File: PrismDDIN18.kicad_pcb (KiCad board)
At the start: 2 copper layers, 280 x 60 mm, 93 parts, among them CON1 BARREL_JACK, IC1 LM2596T-5, J1 Conn_01x03, M1 IN-18, M10 IN-18, Q2 2N7000, Q3 2N7000, Q4 2N7000, Q5 2N7000, Q6 IRF540N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

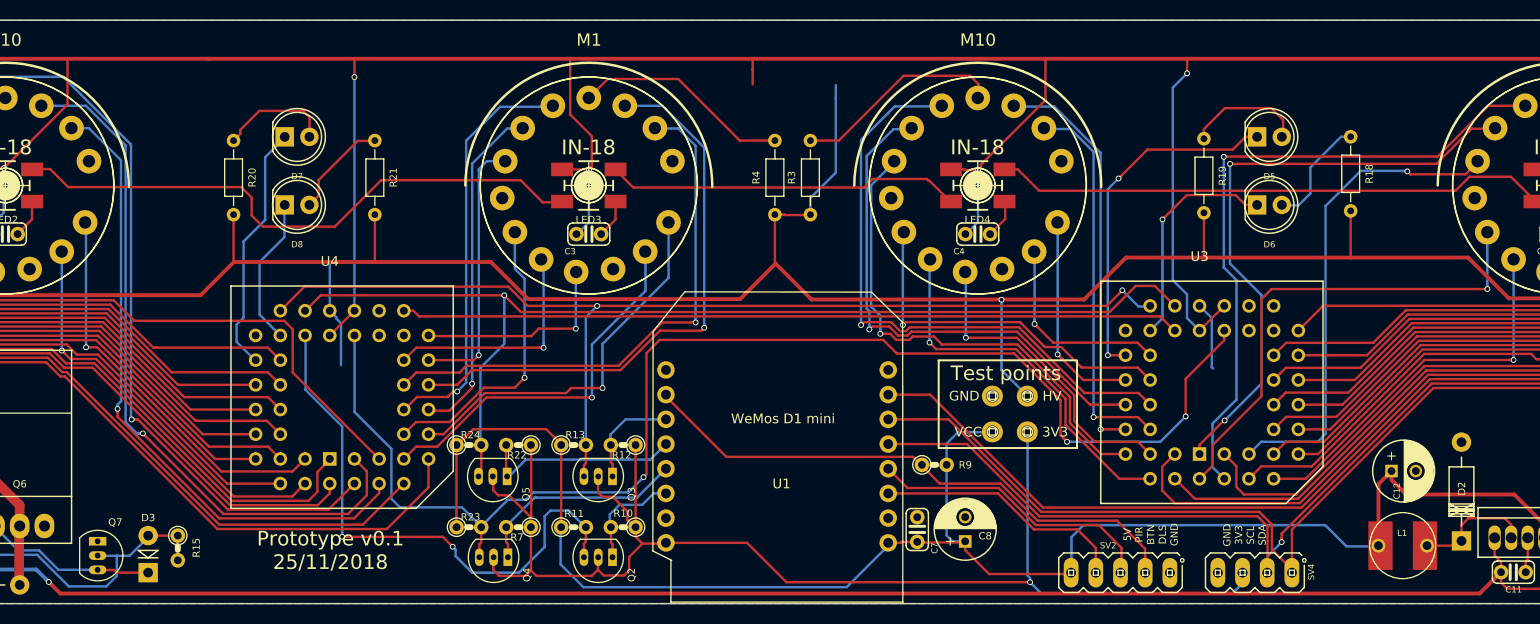
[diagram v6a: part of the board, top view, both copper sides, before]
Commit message: Add centre mouting hole
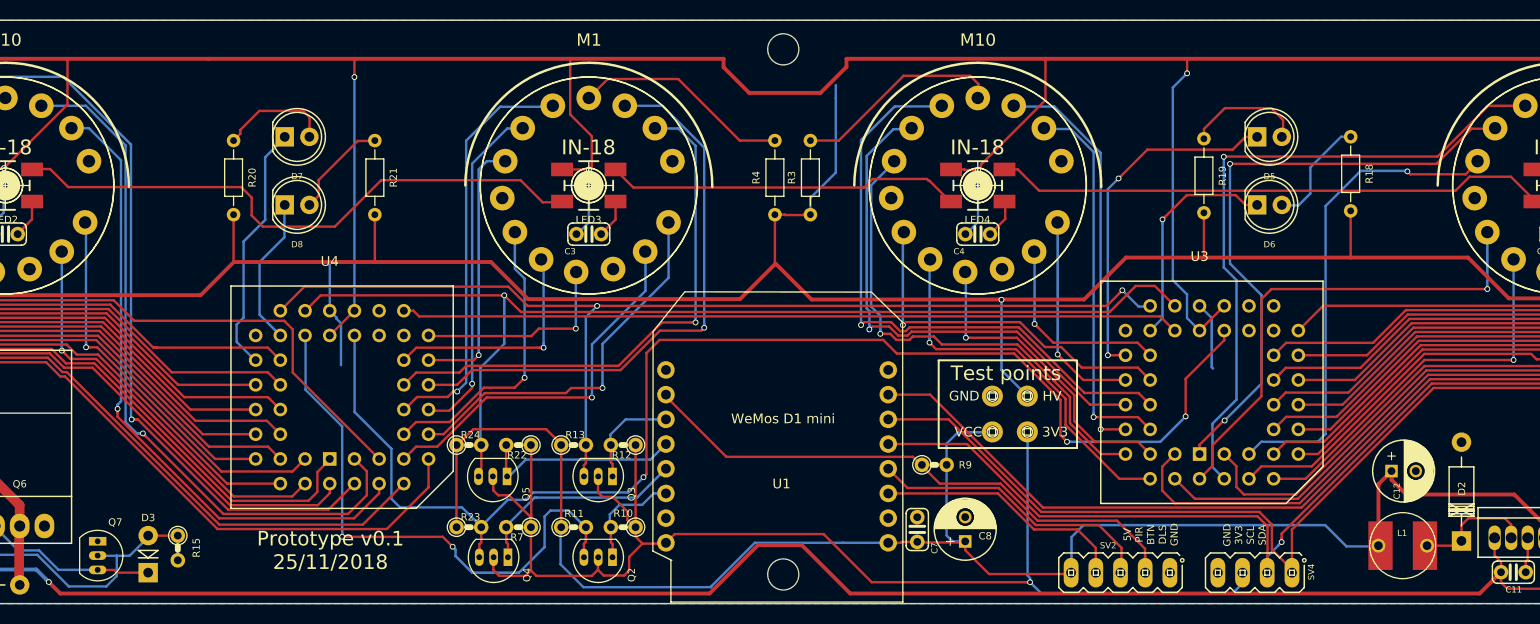
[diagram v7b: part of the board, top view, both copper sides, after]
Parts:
- added MH1: MountingHole_3.2mm_M3, NixieClockMaster:MountingHole_3.2mm_M3, F.Cu at (220.0, 109.0)
- added MH1: MountingHole_3.2mm_M3, NixieClockMaster:MountingHole_3.2mm_M3, F.Cu at (220.0, 163.0)
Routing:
- net /PWR_VIN: track 226.0 -> 230.1 mm
- net /VCC: track 778.1 -> 779.5 mm
- net /3V3: track 140.0 -> 140.8 mm
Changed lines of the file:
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@@
     (thickness 1.6)
     (drawings 17)
-    (tracks 1351)
+    (tracks 1362)
     (zones 0)
-    (modules 93)
+    (modules 95)
     (nets 125)
   )
@@
     (add_net "Net-(U5-Pad7)")
   )
+  (module NixieClockMaster:MountingHole_3.2mm_M3 (layer F.Cu)
+    (at 220 109)
+    (descr "Mounting Hole 3.2mm, no annular, M3")
+    (tags "mounting hole 3.2mm no annular m3")
+    (attr virtual)
+    (fp_text reference MH1 (at 0 -4.2) (layer F.Fab)
+      (effects (font (size 1 1) (thickness 0.15)))
+    )
+    (fp_text value MountingHole_3.2mm_M3 (at 0 4.2) (layer F.Fab)
+      (effects (font (size 1 1) (thickness 0.15)))
+    )
+    (fp_text user %R (at 0.3 0) (layer F.Fab)
+      (effects (font (size 1 1) (thickness 0.15)))
+    )
+    (fp_circle (center 0 0) (end 3.2 0) (layer Cmts.User) (width 0.15))
+    (fp_circle (center 0 0) (end 3.45 0) (layer F.CrtYd) (width 0.05))
+    (pad 1 np_thru_hole circle (at 0 0) (size 3.2 3.2) (drill 3.2) (layers *.Cu *.Mask))
+  )
+  (module NixieClockMaster:MountingHole_3.2mm_M3 (layer F.Cu)
+    (at 220 163)
+    (descr "Mounting Hole 3.2mm, no annular, M3")
+    (tags "mounting hole 3.2mm no annular m3")
+    (attr virtual)
+    (fp_text reference MH1 (at 0 -4.2) (layer F.Fab)
+      (effects (font (size 1 1) (thickness 0.15)))
+    )
+    (fp_text value MountingHole_3.2mm_M3 (at 0 4.2) (layer F.Fab)
+      (effects (font (size 1 1) (thickness 0.15)))
+    )
+    (fp_circle (center 0 0) (end 3.45 0) (layer F.CrtYd) (width 0.05))
+    (fp_circle (center 0 0) (end 3.2 0) (layer Cmts.User) (width 0.15))
+    (fp_text user %R (at 0.3 0) (layer F.Fab)
+      (effects (font (size 1 1) (thickness 0.15)))
+    )
+    (pad 1 np_thru_hole circle (at 0 0) (size 3.2 3.2) (drill 3.2) (layers *.Cu *.Mask))
+  )
   (module NixieClockMaster:C025-024X044 (layer F.Cu)
     (at 100 128)
@@
   (segment (start 241.17 162.96) (end 249.7 162.96) (width 0.25) (layer F.Cu) (net 13) (status 20))
   (segment (start 281.31 160.21) (end 281.36 160.16) (width 0.25) (layer F.Cu) (net 13) (status 30))
-  (segment (start 199.45 164.31) (end 226.52 164.31) (width 0.25) (layer B.Cu) (net 13))
-  (segment (start 226.52 164.31) (end 230.84 159.99) (width 0.25) (layer B.Cu) (net 13) (status 20))
-  (segment (start 197.1 158.14) (end 197.1 161.96) (width 0.25) (layer B.Cu) (net 13) (status 10))
-  (segment (start 197.1 161.96) (end 199.45 164.31) (width 0.25) (layer B.Cu) (net 13))
   (segment (start 175.9 135.88) (end 175.9 111.85) (width 0.25) (layer B.Cu) (net 13) (status 10))
   (segment (start 313.63 147.65) (end 313.63 148.78137) (width 0.25) (layer F.Cu) (net 13) (status 10))
@@
   (segment (start 240.329999 120.850001) (end 246.96 114.22) (width 0.25) (layer F.Cu) (net 13))
   (segment (start 246.96 114.22) (end 246.96 109.97) (width 0.25) (layer F.Cu) (net 13))
-  (segment (start 216.85 111.080657) (end 216.85 109.97) (width 0.25) (layer F.Cu) (net 13))
-  (segment (start 216.8529 111.083557) (end 216.85 111.080657) (width 0.25) (layer F.Cu) (net 13))
-  (segment (start 216.8529 112.6102) (end 216.8529 111.083557) (width 0.25) (layer F.Cu) (net 13) (status 10))
-  (segment (start 246.96 109.97) (end 216.85 109.97) (width 0.4) (layer F.Cu) (net 13))
-  (segment (start 216.85 109.97) (end 198.09 109.97) (width 0.4) (layer F.Cu) (net 13))
   (segment (start 198.09 115.7) (end 198.09 109.97) (width 0.25) (layer F.Cu) (net 13))
   (segment (start 200.309999 117.919999) (end 198.09 115.7) (width 0.25) (layer F.Cu) (net 13))
@@
   (segment (start 186.41 149.77) (end 186.39 149.79) (width 0.25) (layer F.Cu) (net 13))
   (segment (start 186.39 149.79) (end 186.39 158.24) (width 0.25) (layer F.Cu) (net 13))
+  (segment (start 213.86 109.97) (end 213.86 110.84) (width 0.4) (layer F.Cu) (net 13))
+  (segment (start 213.86 109.97) (end 198.09 109.97) (width 0.4) (layer F.Cu) (net 13))
+  (segment (start 213.86 110.84) (end 216.5 113.48) (width 0.4) (layer F.Cu) (net 13))
+  (segment (start 216.5 113.48) (end 223.83 113.48) (width 0.4) (layer F.Cu) (net 13))
+  (segment (start 226.5 110.81) (end 226.5 109.97) (width 0.4) (layer F.Cu) (net 13))
+  (segment (start 223.83 113.48) (end 226.5 110.81) (width 0.4) (layer F.Cu) (net 13))
+  (segment (start 246.96 109.97) (end 226.5 109.97) (width 0.4) (layer F.Cu) (net 13))
+  (segment (start 199.45 164.31) (end 212.57 164.31) (width 0.25) (layer B.Cu) (net 13))
+  (segment (start 197.1 158.14) (end 197.1 161.96) (width 0.25) (layer B.Cu) (net 13))
+  (segment (start 226.14 159.74) (end 230.8 159.74) (width 0.25) (layer B.Cu) (net 13))
+  (segment (start 212.57 164.31) (end 212.57 164.25) (width 0.25) (layer B.Cu) (net 13))
+  (segment (start 212.57 164.25) (end 217.08 159.74) (width 0.25) (layer B.Cu) (net 13))
+  (segment (start 197.1 161.96) (end 199.45 164.31) (width 0.25) (layer B.Cu) (net 13))
+  (segment (start 217.08 159.74) (end 226.14 159.74) (width 0.25) (layer B.Cu) (net 13))
   (segment (start 293.1526 159.8676) (end 293.1526 159.2326) (width 0.25) (layer F.Cu) (net 14) (status 30))
   (segment (start 293.813 162.7693) (end 293.813 161.707834) (width 0.25) (layer F.Cu) (net 14) (status 10))
@@
   (segment (start 301.19 164.47) (end 305.35 160.31) (width 0.25) (layer F.Cu) (net 14) (status 20))
   (via (at 144.47 163.78) (size 0.6) (drill 0.4) (layers F.Cu B.Cu) (net 14))
-  (segment (start 291.62 164.96) (end 293.78 162.8) (width 0.4) (layer F.Cu) (net 14))
-  (segment (start 144.47 163.78) (end 145.65 164.96) (width 0.4) (layer F.Cu) (net 14))
-  (segment (start 145.65 164.96) (end 291.62 164.96) (width 0.4) (layer F.Cu) (net 14))
   (segment (start 123.627999 162.489999) (end 143.179999 162.489999) (width 0.4) (layer B.Cu) (net 14))
   (segment (start 122.428 161.29) (end 123.627999 162.489999) (width 0.4) (layer B.Cu) (net 14))
   (segment (start 144.170001 163.480001) (end 144.47 163.78) (width 0.4) (layer B.Cu) (net 14))
   (segment (start 143.179999 162.489999) (end 144.170001 163.480001) (width 0.4) (layer B.Cu) (net 14))
+  (segment (start 291.62 164.96) (end 293.78 162.8) (width 0.4) (layer F.Cu) (net 14))
+  (segment (start 144.47 163.78) (end 145.65 164.96) (width 0.4) (layer F.Cu) (net 14))
+  (segment (start 226.89 164.96) (end 291.62 164.96) (width 0.4) (layer F.Cu) (net 14))
+  (segment (start 145.65 164.96) (end 212.42 164.96) (width 0.4) (layer F.Cu) (net 14))
+  (segment (start 212.42 164.96) (end 217.39 159.99) (width 0.4) (layer F.Cu) (net 14))
+  (segment (start 217.39 159.99) (end 221.92 159.99) (width 0.4) (layer F.Cu) (net 14))
+  (segment (start 221.92 159.99) (end 226.89 164.96) (width 0.4) (layer F.Cu) (net 14))
   (segment (start 94.488 150.006032) (end 96.881968 152.4) (width 1) (layer F.Cu) (net 15))
   (segment (start 94.488 148.59254) (end 94.488 150.006032) (width 1) (layer F.Cu) (net 15) (status 10))
@@
   (segment (start 190.68 154.86) (end 190.18 154.36) (width 0.25) (layer F.Cu) (net 118))
   (segment (start 190.18 154.36) (end 190.18 152.94) (width 0.25) (layer F.Cu) (net 118) (status 20))
-  (segment (start 207.93479 159.74924) (end 216.27924 159.74924) (width 0.25) (layer F.Cu) (net 118))
-  (segment (start 216.27924 159.74924) (end 220.33 163.8) (width 0.25) (layer F.Cu) (net 118))
   (via (at 245.38 163.8) (size 0.6) (drill 0.4) (layers F.Cu B.Cu) (net 118))
-  (segment (start 220.33 163.8) (end 245.38 163.8) (width 0.25) (layer F.Cu) (net 118))
   (segment (start 245.679999 164.099999) (end 245.38 163.8) (width 0.25) (layer B.Cu) (net 118))
   (segment (start 246.54 164.96) (end 245.679999 164.099999) (width 0.25) (layer B.Cu) (net 118))
@@
   (segment (start 194.05 162.59) (end 194.61 163.15) (width 0.25) (layer F.Cu) (net 118))
   (segment (start 194.61 163.15) (end 200.31 163.15) (width 0.25) (layer F.Cu) (net 118))
+  (segment (start 208.834789 158.849241) (end 224.149241 158.849241) (width 0.25) (layer F.Cu) (net 118))
+  (segment (start 207.93479 159.74924) (end 208.834789 158.849241) (width 0.25) (layer F.Cu) (net 118))
+  (segment (start 244.955736 163.8) (end 245.38 163.8) (width 0.25) (layer F.Cu) (net 118))
+  (segment (start 229.1 163.8) (end 244.955736 163.8) (width 0.25) (layer F.Cu) (net 118))
+  (segment (start 224.149241 158.849241) (end 229.1 163.8) (width 0.25) (layer F.Cu) (net 118))
   (segment (start 202.27 152.87) (end 202.17 152.97) (width 0.25) (layer F.Cu) (net 119) (status 30))
   (segment (start 202.22 148.62) (end 202.22 149.74) (width 0.25) (layer B.Cu) (net 119))

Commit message: Update netlist, bodard date
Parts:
- C12: value 220uF -> 220uF 10V
- C16, C17: value 220uF -> 220uF 35V
- C20: value 2.2uF -> 2.2uF 400V
- C21: value C -> 100nF
- H1, H10, M1, M10, S1, S10: footprint NixieClockMaster:IN-18 -> NixieClockMaster:IN-18-Small-Hole
- Q6: value IRF540N -> IRF640
- Q7: value Q_PNP_BCE -> 2N3906
- R15: value R -> 1k
- RV1: value 1k -> 5k
- Y1: value Crystal_Small -> 32.768kHz
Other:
- board text added: "Prototype v0.1 25/02/2019"
- board text removed: "Prototype v0.1 25/11/2018"
